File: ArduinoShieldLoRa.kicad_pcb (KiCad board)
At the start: 2 copper layers, 68.6 x 53.3 mm, 19 parts, among them J1 CONN_01X03, P1 Power, P2 Analog, P3 Digital, P4 Digital, P5 CONN_01X01, P6 CONN_01X01, P7 CONN_01X01, P8 CONN_01X01, U1 RFM95, U2 74HC4050D, U3 AP2112K-3.3

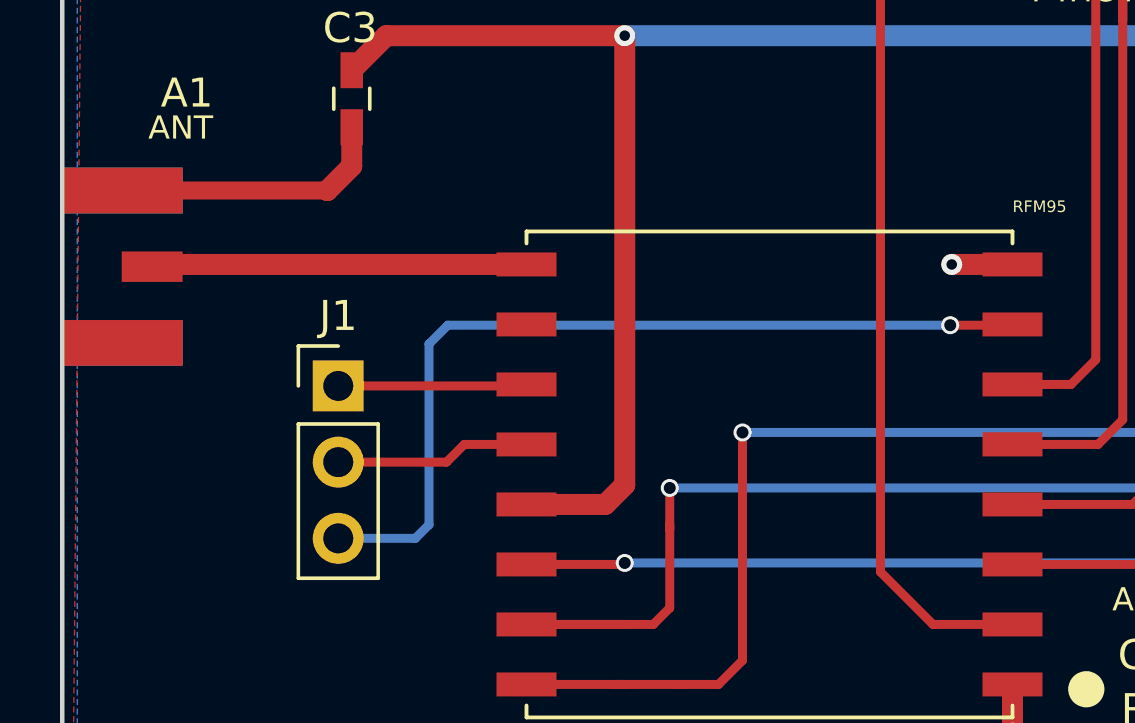
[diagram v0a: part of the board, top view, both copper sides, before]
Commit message: add pin for cable as antenna
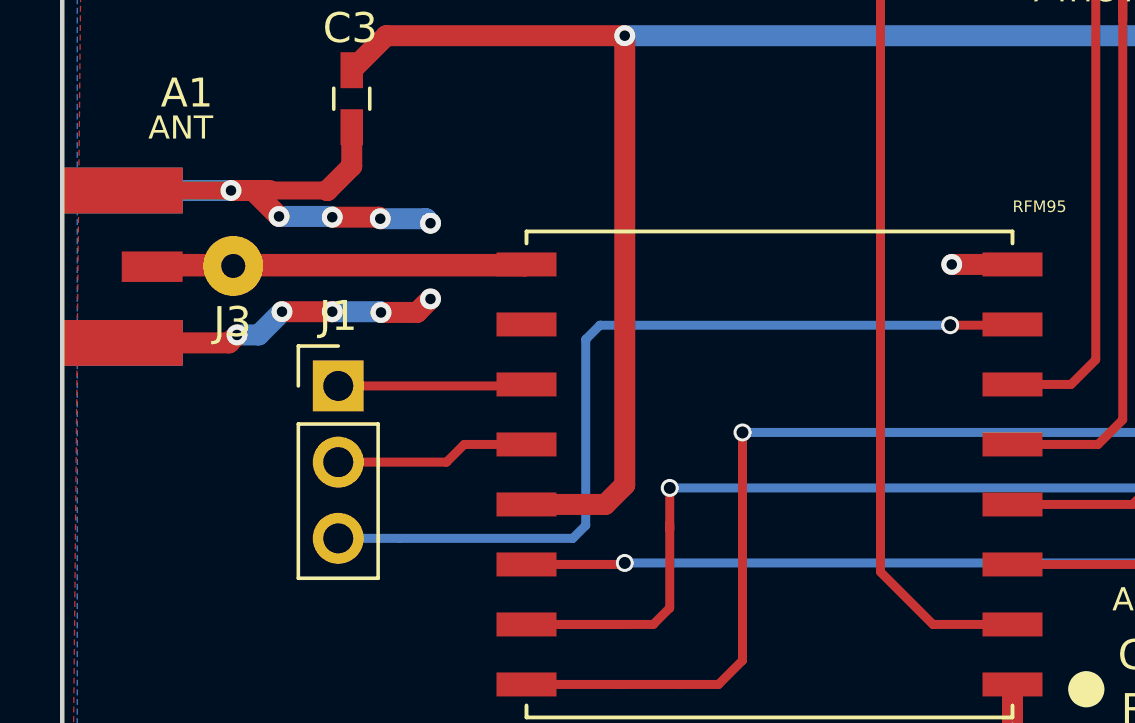
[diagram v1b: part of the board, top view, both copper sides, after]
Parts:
- added J3: CONN_01X01, Wire_Pads:SolderWirePad_single_0-8mmDrill, F.Cu at (116.7, 102.6)
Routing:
- net GND: track 23.3 -> 44.9 mm, vias 5 -> 15
- net Net-(A1-Pad1): track 12.6 -> 25.2 mm
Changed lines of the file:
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@@
 (kicad_pcb (version 4) (host pcbnew 4.0.6)
   (general
-    (links 42)
-    (no_connects 0)
+    (links 43)
+    (no_connects 13)
     (area 110.922999 72.949999 179.653001 126.440001)
     (thickness 1.6)
     (drawings 27)
-    (tracks 173)
+    (tracks 208)
     (zones 0)
-    (modules 19)
+    (modules 20)
     (nets 52)
   )
@@
     )
   )
+  (module Wire_Pads:SolderWirePad_single_0-8mmDrill (layer F.Cu)
+    (at 116.698 102.59)
+    (fp_text reference J3 (at -0.025 1.875) (layer F.SilkS)
+      (effects (font (size 1 1) (thickness 0.15)))
+    )
+    (fp_text value CONN_01X01 (at 0 2.54) (layer F.Fab)
+      (effects (font (size 1 1) (thickness 0.15)))
+    )
+    (pad 1 thru_hole circle (at 0 0) (size 1.99898 1.99898) (drill 0.8001) (layers *.Cu *.Mask)
+      (net 33 "Net-(A1-Pad1)"))
+  )
   (gr_text 1 (at 138.938 121.285 90) (layer F.SilkS)
     (effects (font (size 1 1) (thickness 0.15)))
@@
   (segment (start 149.148 112.6651) (end 149.148 115.465) (width 0.6) (layer F.Cu) (net 3))
   (segment (start 149.148 115.465) (end 149.048 115.565) (width 0.6) (layer F.Cu) (net 3))
+  (segment (start 121.598 101.015) (end 123.123 101.015) (width 0.7) (layer B.Cu) (net 4))
+  (segment (start 123.123 101.015) (end 123.273 101.165) (width 0.7) (layer B.Cu) (net 4))
+  (via (at 123.273 101.165) (size 0.7) (drill 0.35) (layers F.Cu B.Cu) (net 4))
+  (segment (start 119.998 100.965) (end 121.548 100.965) (width 0.7) (layer F.Cu) (net 4))
+  (via (at 121.598 101.015) (size 0.7) (drill 0.35) (layers F.Cu B.Cu) (net 4))
+  (segment (start 121.548 100.965) (end 121.598 101.015) (width 0.7) (layer F.Cu) (net 4))
+  (segment (start 118.223 100.94) (end 119.973 100.94) (width 0.7) (layer B.Cu) (net 4))
+  (segment (start 119.973 100.94) (end 119.998 100.965) (width 0.7) (layer B.Cu) (net 4))
+  (via (at 119.998 100.965) (size 0.7) (drill 0.35) (layers F.Cu B.Cu) (net 4))
+  (segment (start 116.623 100.075) (end 117.358 100.075) (width 0.7) (layer F.Cu) (net 4))
+  (segment (start 117.358 100.075) (end 118.223 100.94) (width 0.7) (layer F.Cu) (net 4))
+  (via (at 118.223 100.94) (size 0.7) (drill 0.35) (layers F.Cu B.Cu) (net 4))
+  (segment (start 117.923 100.075) (end 119.823 100.075) (width 0.6) (layer F.Cu) (net 4))
+  (segment (start 116.623 100.075) (end 117.923 100.075) (width 0.7) (layer F.Cu) (net 4))
+  (segment (start 112.98 100.075) (end 116.623 100.075) (width 0.6) (layer F.Cu) (net 4))
+  (via (at 116.623 100.075) (size 0.7) (drill 0.35) (layers F.Cu B.Cu) (net 4))
+  (segment (start 112.98 100.075) (end 116.623 100.075) (width 0.7) (layer B.Cu) (net 4))
+  (segment (start 121.623 104.14) (end 122.823 104.14) (width 0.7) (layer F.Cu) (net 4))
+  (segment (start 122.823 104.14) (end 123.273 103.69) (width 0.7) (layer F.Cu) (net 4))
+  (via (at 123.273 103.69) (size 0.7) (drill 0.35) (layers F.Cu B.Cu) (net 4))
+  (segment (start 119.998 104.115) (end 121.598 104.115) (width 0.7) (layer B.Cu) (net 4))
+  (segment (start 121.598 104.115) (end 121.623 104.14) (width 0.7) (layer B.Cu) (net 4))
+  (via (at 121.623 104.14) (size 0.7) (drill 0.35) (layers F.Cu B.Cu) (net 4))
+  (segment (start 118.323 104.115) (end 119.998 104.115) (width 0.7) (layer F.Cu) (net 4))
+  (via (at 119.998 104.115) (size 0.7) (drill 0.35) (layers F.Cu B.Cu) (net 4))
+  (segment (start 116.823 104.89) (end 117.548 104.89) (width 0.7) (layer B.Cu) (net 4))
+  (segment (start 117.548 104.89) (end 118.323 104.115) (width 0.7) (layer B.Cu) (net 4))
+  (via (at 118.323 104.115) (size 0.7) (drill 0.35) (layers F.Cu B.Cu) (net 4))
+  (segment (start 112.98 105.155) (end 116.558 105.155) (width 0.7) (layer F.Cu) (net 4))
+  (segment (start 116.558 105.155) (end 116.823 104.89) (width 0.7) (layer F.Cu) (net 4))
+  (via (at 116.823 104.89) (size 0.7) (drill 0.35) (layers F.Cu B.Cu) (net 4))
   (segment (start 142.673 102.54) (end 140.648 102.54) (width 0.7) (layer F.Cu) (net 4))
   (via (at 140.648 102.54) (size 0.7) (drill 0.35) (layers F.Cu B.Cu) (net 4))
   (segment (start 142.673 116.54) (end 142.673 118.165) (width 0.7) (layer F.Cu) (net 4))
   (via (at 142.673 118.165) (size 0.7) (drill 0.35) (layers F.Cu B.Cu) (net 4))
-  (segment (start 112.98 100.075) (end 119.823 100.075) (width 0.6) (layer F.Cu) (net 4))
   (segment (start 120.648 97.965) (end 120.648 99.265) (width 0.7) (layer F.Cu) (net 4))
   (segment (start 120.648 99.265) (end 119.838 100.075) (width 0.7) (layer F.Cu) (net 4))
@@
   (segment (start 151.648 91.165) (end 152.498 90.315) (width 0.3) (layer F.Cu) (net 32))
   (segment (start 149.498 91.165) (end 151.648 91.165) (width 0.3) (layer F.Cu) (net 32))
+  (segment (start 116.698 102.59) (end 126.423 102.59) (width 0.7) (layer F.Cu) (net 33))
+  (segment (start 126.423 102.59) (end 126.473 102.54) (width 0.7) (layer F.Cu) (net 33))
+  (segment (start 116.698 102.59) (end 114.021 102.59) (width 0.7) (layer F.Cu) (net 33))
+  (segment (start 114.021 102.59) (end 113.996 102.615) (width 0.7) (layer F.Cu) (net 33))
   (segment (start 126.473 102.54) (end 114.071 102.54) (width 0.7) (layer F.Cu) (net 33))
   (segment (start 114.071 102.54) (end 113.996 102.615) (width 0.7) (layer F.Cu) (net 33))
@@
   (segment (start 124.398 108.54) (end 126.473 108.54) (width 0.3) (layer F.Cu) (net 35))
   (segment (start 120.198 109.13) (end 123.808 109.13) (width 0.3) (layer F.Cu) (net 35))
+  (segment (start 140.598 104.565) (end 128.923 104.565) (width 0.3) (layer B.Cu) (net 36))
+  (segment (start 128.923 104.565) (end 128.448 105.04) (width 0.3) (layer B.Cu) (net 36))
+  (segment (start 128.448 105.04) (end 128.448 111.24) (width 0.3) (layer B.Cu) (net 36))
+  (segment (start 128.448 111.24) (end 128.018 111.67) (width 0.3) (layer B.Cu) (net 36))
+  (segment (start 128.018 111.67) (end 122.248 111.67) (width 0.3) (layer B.Cu) (net 36))
+  (segment (start 122.248 111.67) (end 120.198 111.67) (width 0.3) (layer B.Cu) (net 36))
   (segment (start 140.598 104.565) (end 142.648 104.565) (width 0.3) (layer F.Cu) (net 36))
   (segment (start 142.648 104.565) (end 142.673 104.54) (width 0.3) (layer F.Cu) (net 36))
-  (segment (start 123.223 105.19) (end 123.848 104.565) (width 0.3) (layer B.Cu) (net 36))
-  (segment (start 123.848 104.565) (end 140.598 104.565) (width 0.3) (layer B.Cu) (net 36))
   (via (at 140.598 104.565) (size 0.6) (drill 0.4) (layers F.Cu B.Cu) (net 36))
-  (segment (start 123.223 111.215) (end 123.223 105.19) (width 0.3) (layer B.Cu) (net 36))
-  (segment (start 122.768 111.67) (end 123.223 111.215) (width 0.3) (layer B.Cu) (net 36))
-  (segment (start 120.198 111.67) (end 122.768 111.67) (width 0.3) (layer B.Cu) (net 36))
   (segment (start 152.598 117.215) (end 152.448 117.365) (width 0.3) (layer F.Cu) (net 37))
   (segment (start 152.448 117.365) (end 151.248 117.365) (width 0.3) (layer F.Cu) (net 37))

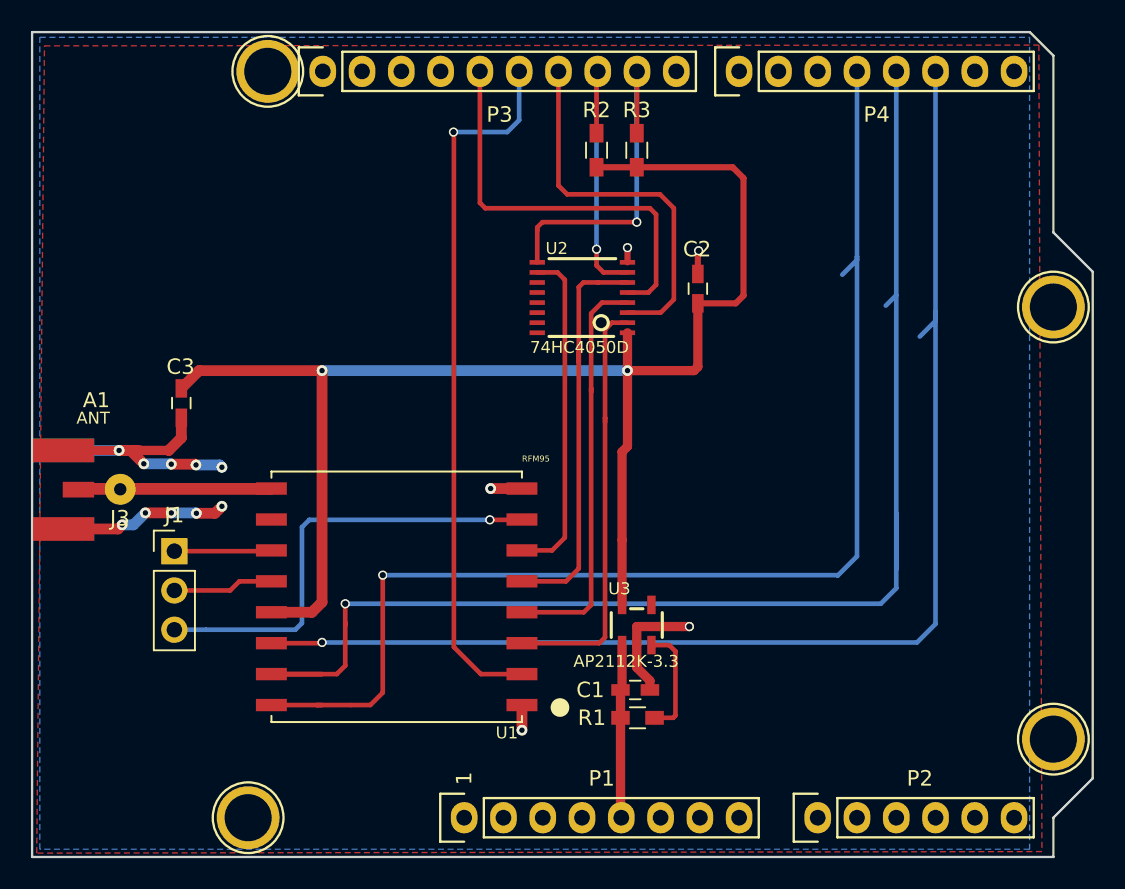
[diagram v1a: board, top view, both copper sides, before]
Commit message: Added logos
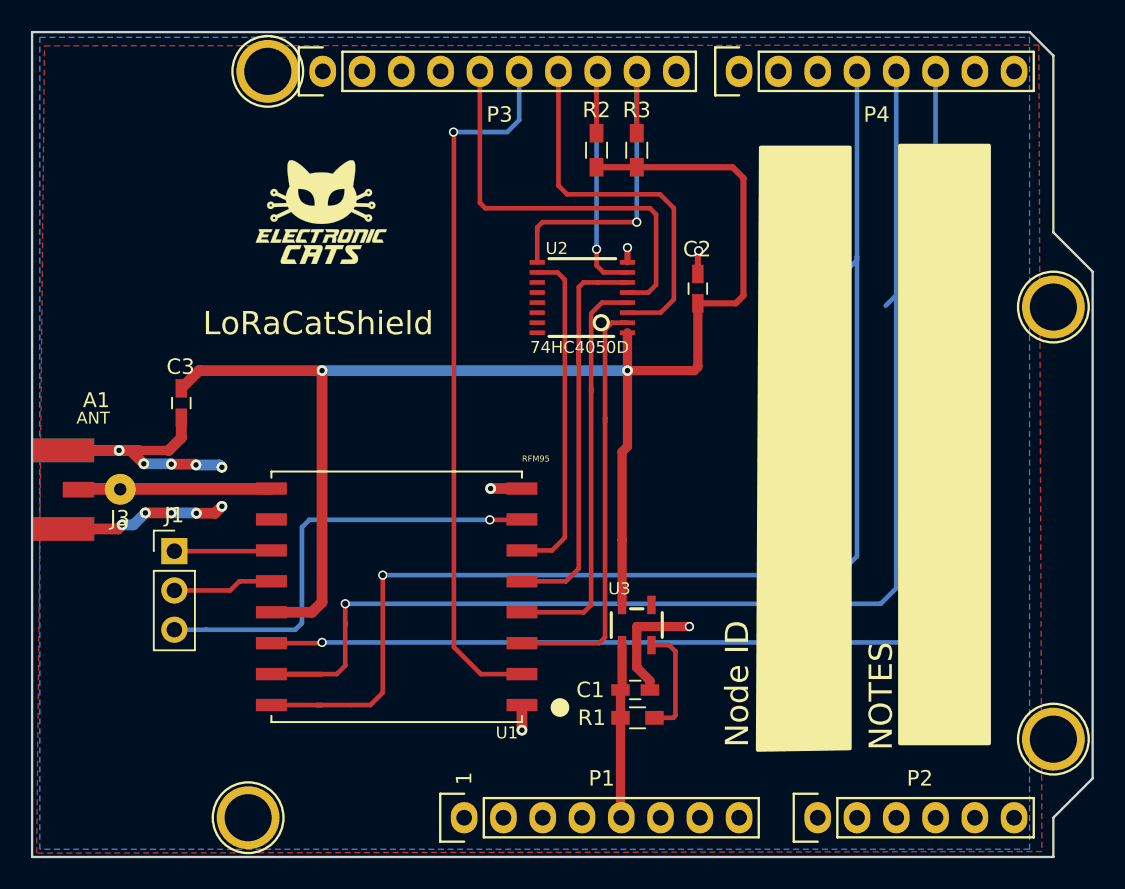
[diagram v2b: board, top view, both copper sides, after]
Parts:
- added G***: LOGO, TIH:electronic_cats_logo_8x6, F.Cu at (129.7, 84.7)
- added REF***: OSHW-Logo2_9.8x8mm_SilkScreen, Symbols:OSHW-Logo2_9.8x8mm_SilkScreen, B.Cu at (146.6, 99.9)
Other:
- board text added: "LoRaCatShield"
- board text added: "NOTES"
- board text added: "Node ID"
- board text added: "Version 0.3"
